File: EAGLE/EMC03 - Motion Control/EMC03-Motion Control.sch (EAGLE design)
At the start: 62 parts, among them J1 HR911105A, J2 SWD, J3 UART0, J6 USB-B, Q2 25MHz, U1 LPC1768, U2 USD-SOCKETSMD, U3 CPL-ETH-PHY-LAN8720A, U4 74LVC1G04, U5 TC1015-3.3VCT713, U6 SP3485

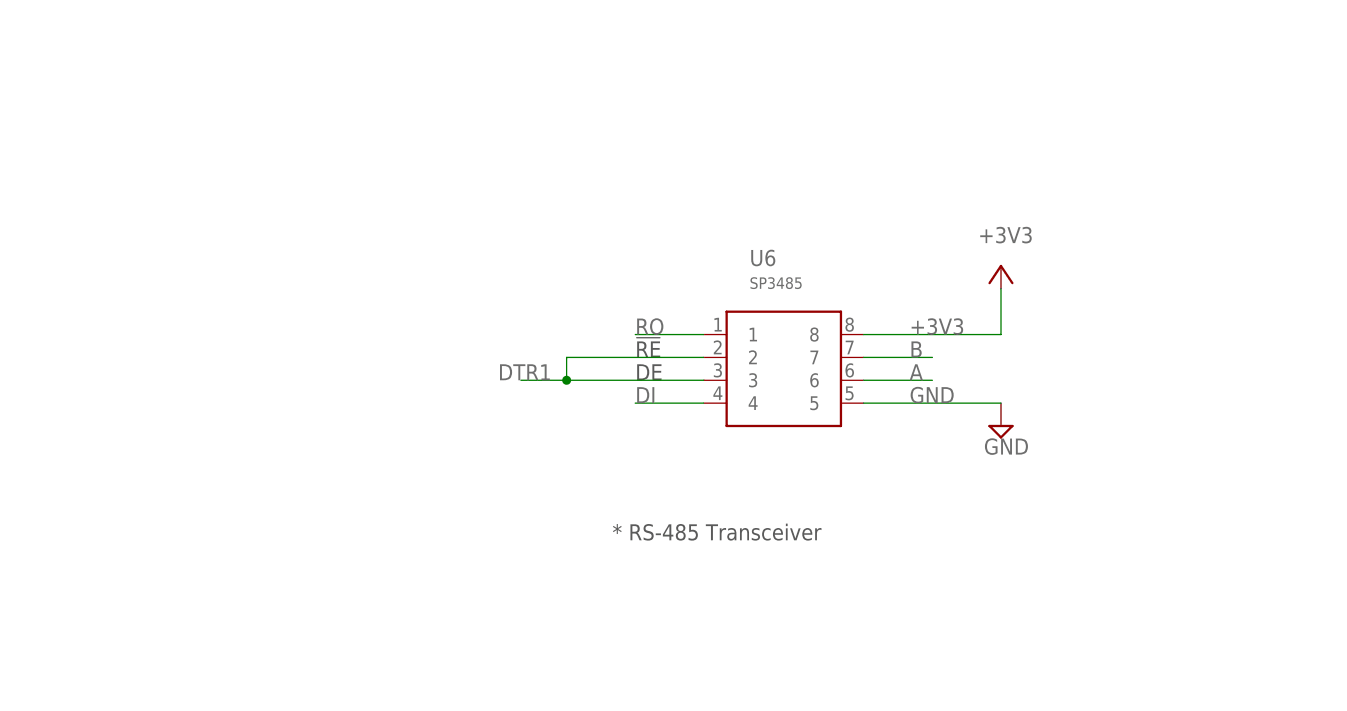
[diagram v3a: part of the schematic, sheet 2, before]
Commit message: Fixed connections for RS-485, added resistors for fail-safe mode and termination. Created RJ-45 device for RS-485 connection. Added LED device and placed on schematic 7 LEDs (4 green, 3 red). Created devices for pushbuttons. Created circuits for DFU and ISP_COM.
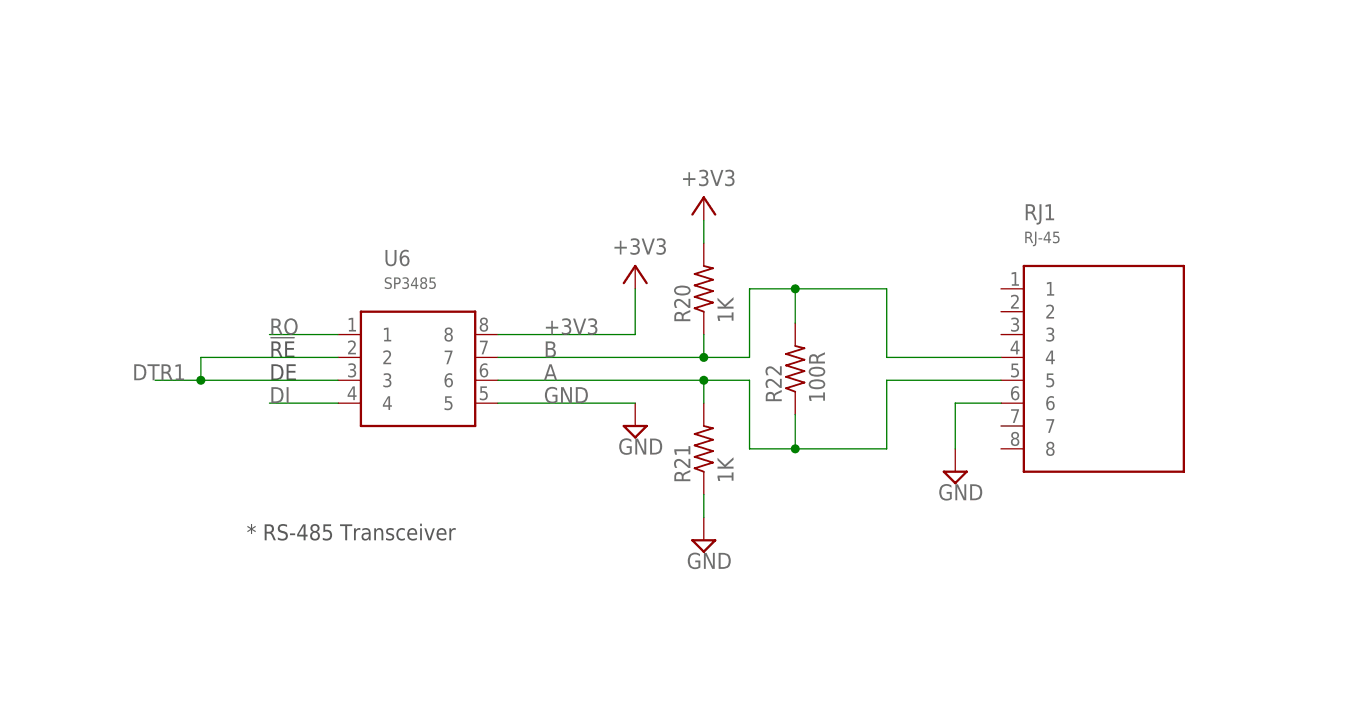
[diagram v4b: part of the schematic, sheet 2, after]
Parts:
- added LED1, LED2, LED3, LED4: GREEN, TinWhiskers:CPL-LED-0603-GREEN
- added LED5, LED6, LED7: RED, TinWhiskers:CPL-LED-0603-RED
- added R20, R21: 1K, TinWhiskers:CPL-RES-0603-1K-0.1W
- added R22: 100R, TinWhiskers:CPL-RES-0603-100-0.1W
- added R23, R24: 10k, TinWhiskers:CPL-RES-0603-10K-0.1W
- added RJ1: RJ-45, TinWhiskers:CPL-CON-MOD-RJ45
- added S2, S3: 147873-2, TinWhiskers:CPL-SW-MOM-0603
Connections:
- new net DFU: R24.1, S3.2, U1.P0-11
- new net ISP_COM: R23.1, S2.2, U1.P0-10
- net +3V3: now also R20.2, R23.2, R24.2
- net A: now also R21.2, R22.1, RJ1.5
- net B: now also R20.1, R22.2, RJ1.4
- net GND: now also R21.1, RJ1.6, S2.1, S3.1
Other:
- moved on the sheet: U6

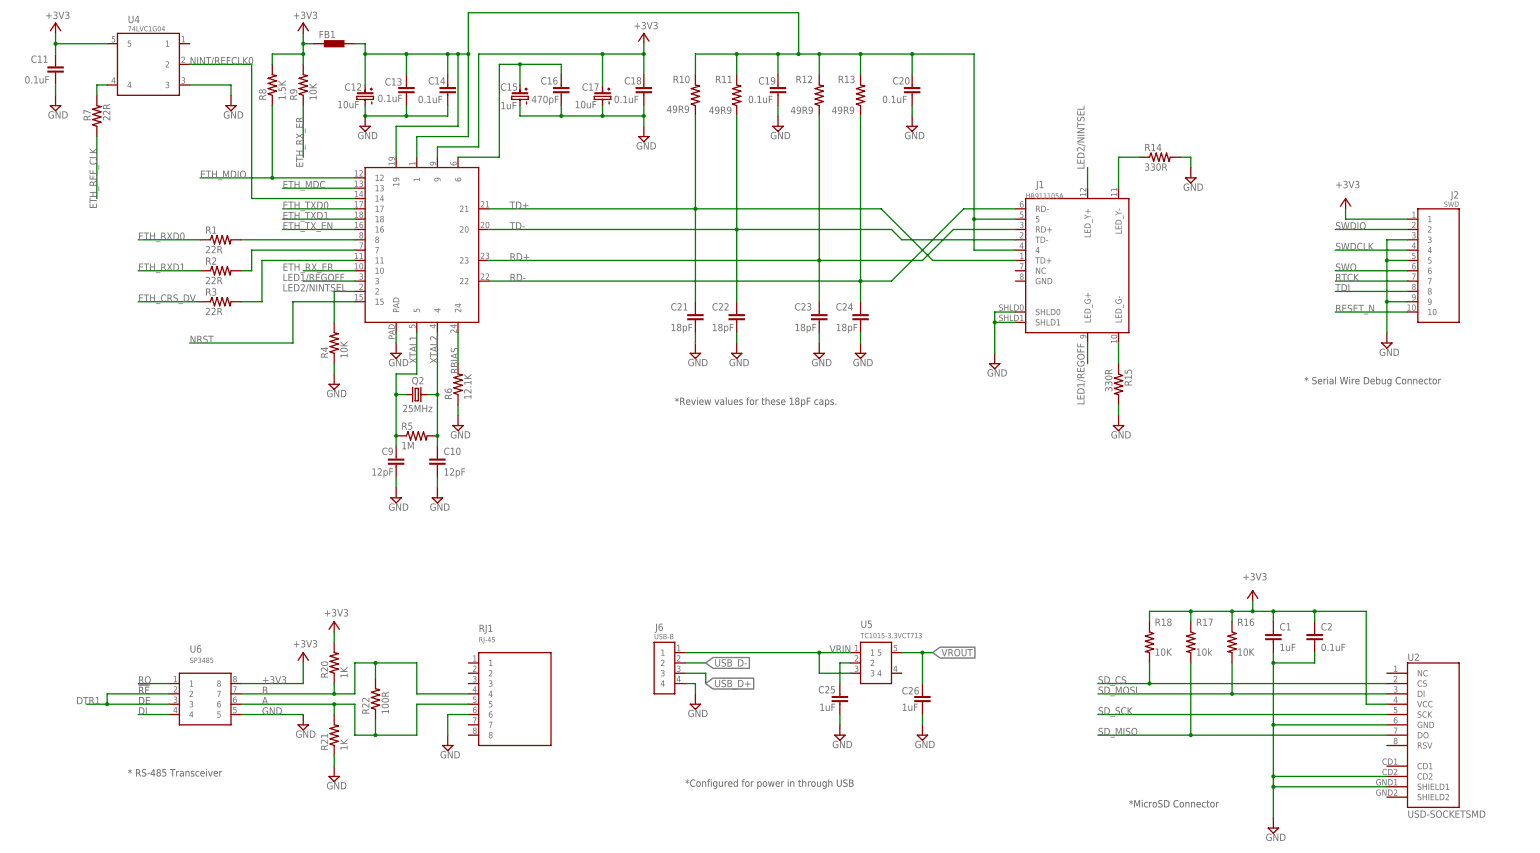
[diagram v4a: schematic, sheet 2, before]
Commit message: Schematic has been updated to assist with sourcing, cleaned up Refdes'.
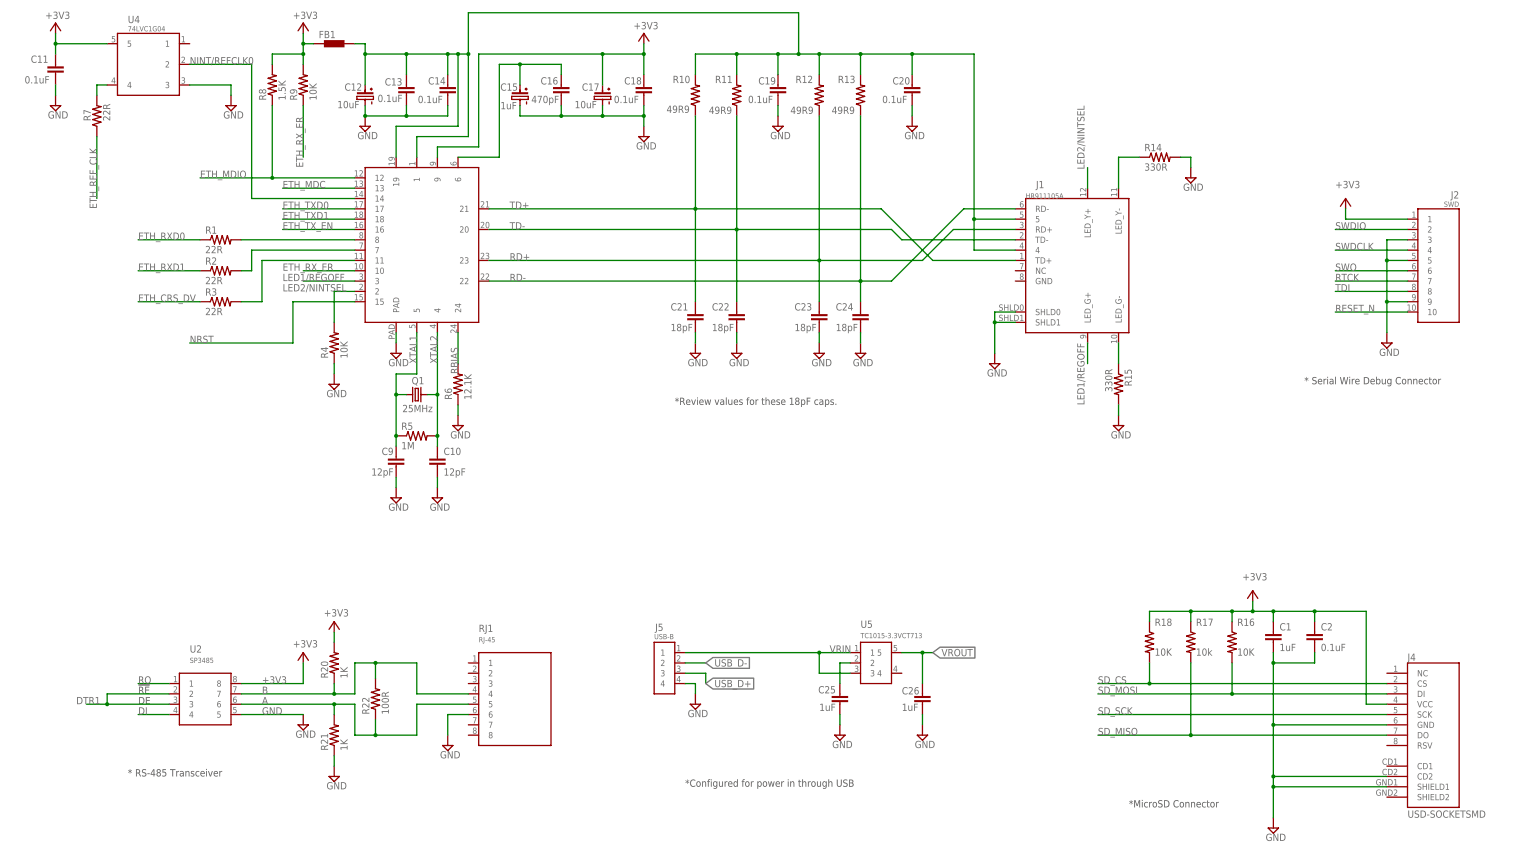
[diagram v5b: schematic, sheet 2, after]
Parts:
- removed U6: SP3485, TinWhiskers:SP3485
- added J4: USD-SOCKETSMD, TinWhiskers:USD-SOCKETSMD
- U2: value USD-SOCKETSMD -> SP3485; device TinWhiskers:USD-SOCKETSMD -> TinWhiskers:SP3485
- renumbered J6 to J5, Q2 to Q1
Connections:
- net +3V3: now also J4.VCC, U2.8; no longer U2.VCC, U6.8
- net A: now also U2.6; no longer U6.6
- net B: now also U2.7; no longer U6.7
- net DI: now also U2.4; no longer U6.4
- net DTR1: now also U2.2, U2.3; no longer U6.2, U6.3
- net GND: now also J4.CD2, J4.GND, J4.SHIELD1, U2.5; no longer U2.CD2, U2.GND, U2.SHIELD1, U6.5
- net RO: now also U2.1; no longer U6.1
- net SD_CS: now also J4.CS; no longer U2.CS
- net SD_MISO: now also J4.DO; no longer U2.DO
- net SD_MOSI: now also J4.DI; no longer U2.DI
- net SD_SCK: now also J4.SCK; no longer U2.SCK
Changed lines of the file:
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@@
 <setting verticaltext="up"/>
 </settings>
-<grid distance="0.1" unitdist="inch" unit="inch" style="lines" multiple="1" display="yes" altdistance="0.025" altunitdist="inch" altunit="inch"/>
+<grid distance="0.1" unitdist="inch" unit="inch" style="lines" multiple="1" display="no" altdistance="0.01" altunitdist="inch" altunit="inch"/>
 <layers>
 <layer number="1" name="Top" color="4" fill="1" visible="no" active="no"/>
@@
 <part name="R3" library="TinWhiskers" deviceset="CPL-RES-0603-22R-0.1W" device="" value="22R"/>
 <part name="SUPPLY3" library="TinWhiskers" deviceset="GND" device=""/>
-<part name="Q2" library="TinWhiskers" deviceset="CPL-OSC-CRY-25MHZ-18PF" device="" value="25MHz"/>
+<part name="Q1" library="TinWhiskers" deviceset="CPL-OSC-CRY-25MHZ-18PF" device="" value="25MHz"/>
 <part name="C9" library="TinWhiskers" deviceset="CPL-CAP-C0G-0603-12PF-50V" device="" value="12pF"/>
 <part name="C10" library="TinWhiskers" deviceset="CPL-CAP-C0G-0603-12PF-50V" device="" value="12pF"/>
@@
 <part name="SUPPLY4" library="TinWhiskers" deviceset="GND" device=""/>
 <part name="SUPPLY5" library="TinWhiskers" deviceset="GND" device=""/>
-<part name="U2" library="TinWhiskers" deviceset="USD-SOCKET" device="SMD"/>
+<part name="J4" library="TinWhiskers" deviceset="USD-SOCKET" device="SMD"/>
 <part name="C1" library="TinWhiskers" deviceset="CPL-CAP-X5R-0603-1UF-50V" device="" value="1uF"/>
 <part name="C2" library="TinWhiskers" deviceset="CPL-CAP-X5R-0603-0.1UF-35V" device="" value="0.1uF"/>
@@
 <part name="+3V4" library="supply1" deviceset="+3V3" device=""/>
 <part name="SUPPLY6" library="TinWhiskers" deviceset="GND" device=""/>
-<part name="J6" library="TinWhiskers" deviceset="CPL-CON-USB-B" device="" value="USB-B"/>
+<part name="J5" library="TinWhiskers" deviceset="CPL-CON-USB-B" device="" value="USB-B"/>
 <part name="U5" library="TinWhiskers" deviceset="CPL-REG-LIN-3.3V-0.1A" device="" value="TC1015-3.3VCT713"/>
 <part name="SUPPLY14" library="TinWhiskers" deviceset="GND" device=""/>
@@
 <part name="+3V5" library="supply1" deviceset="+3V3" device=""/>
 <part name="SUPPLY21" library="TinWhiskers" deviceset="GND" device=""/>
-<part name="U6" library="TinWhiskers" deviceset="SP3485" device=""/>
+<part name="U2" library="TinWhiskers" deviceset="SP3485" device=""/>
 <part name="+3V6" library="supply1" deviceset="+3V3" device=""/>
 <part name="SUPPLY24" library="TinWhiskers" deviceset="GND" device=""/>
@@
 </instance>
 <instance part="SUPPLY3" gate="GND" x="99.06" y="165.1"/>
-<instance part="Q2" gate="G$1" x="104.14" y="154.94" smashed="yes">
+<instance part="Q1" gate="G$1" x="104.14" y="154.94" smashed="yes">
 <attribute name="NAME" x="102.87" y="157.48" size="1.778" layer="95"/>
 <attribute name="VALUE" x="100.584" y="150.622" size="1.778" layer="96"/>
@@
 <instance part="SUPPLY4" gate="GND" x="294.64" y="208.28"/>
 <instance part="SUPPLY5" gate="GND" x="276.86" y="147.32"/>
-<instance part="U2" gate="G$1" x="350.52" y="73.66"/>
+<instance part="J4" gate="G$1" x="350.52" y="73.66"/>
 <instance part="C1" gate="G$1" x="314.96" y="96.52" smashed="yes" rot="R90">
 <attribute name="NAME" x="316.484" y="96.901" size="1.778" layer="95"/>
@@
 </instance>
 <instance part="SUPPLY6" gate="GND" x="314.96" y="48.26"/>
-<instance part="J6" gate="G$1" x="167.64" y="88.9" smashed="yes">
+<instance part="J5" gate="G$1" x="167.64" y="88.9" smashed="yes">
 <attribute name="NAME" x="162.814" y="96.774" size="1.778" layer="95" font="vector" ratio="12"/>
 <attribute name="VALUE" x="162.56" y="94.742" size="1.27" layer="95" font="vector" ratio="10"/>
@@
 </instance>
 <instance part="SUPPLY21" gate="GND" x="342.9" y="167.64"/>
-<instance part="U6" gate="G$1" x="48.26" y="78.74"/>
+<instance part="U2" gate="G$1" x="48.26" y="78.74"/>
 <instance part="+3V6" gate="G$1" x="76.2" y="91.44" smashed="yes">
 <attribute name="VALUE" x="73.66" y="92.71" size="1.778" layer="96"/>
@@
 <junction x="314.96" y="88.9"/>
 <pinref part="SUPPLY6" gate="GND" pin="GND"/>
-<pinref part="U2" gate="G$1" pin="GND"/>
+<pinref part="J4" gate="G$1" pin="GND"/>
 <wire x1="314.96" y1="73.66" x2="314.96" y2="60.96" width="0.1524" layer="91"/>
 <wire x1="314.96" y1="60.96" x2="314.96" y2="58.42" width="0.1524" layer="91"/>
@@
 <wire x1="342.9" y1="73.66" x2="314.96" y2="73.66" width="0.1524" layer="91"/>
 <junction x="314.96" y="73.66"/>
-<pinref part="U2" gate="G$1" pin="CD2"/>
+<pinref part="J4" gate="G$1" pin="CD2"/>
 <wire x1="342.9" y1="60.96" x2="314.96" y2="60.96" width="0.1524" layer="91"/>
 <junction x="314.96" y="60.96"/>
-<pinref part="U2" gate="G$1" pin="SHIELD1"/>
+<pinref part="J4" gate="G$1" pin="SHIELD1"/>
 <wire x1="342.9" y1="58.42" x2="314.96" y2="58.42" width="0.1524" layer="91"/>
 <junction x="314.96" y="58.42"/>
 </segment>
 <segment>
-<pinref part="J6" gate="G$1" pin="4"/>
+<pinref part="J5" gate="G$1" pin="4"/>
 <wire x1="170.18" y1="83.82" x2="172.72" y2="83.82" width="0.1524" layer="91"/>
 <wire x1="172.72" y1="83.82" x2="172.72" y2="81.28" width="0.1524" layer="91"/>
@@
 </segment>
 <segment>
-<pinref part="U6" gate="G$1" pin="5"/>
+<pinref part="U2" gate="G$1" pin="5"/>
 <label x="66.04" y="76.2" size="1.778" layer="95"/>
 <pinref part="SUPPLY24" gate="GND" pin="GND"/>
@@
 <wire x1="104.14" y1="160.02" x2="99.06" y2="160.02" width="0.1524" layer="91"/>
 <wire x1="99.06" y1="160.02" x2="99.06" y2="154.94" width="0.1524" layer="91"/>
-<pinref part="Q2" gate="G$1" pin="1"/>
+<pinref part="Q1" gate="G$1" pin="1"/>
 <wire x1="99.06" y1="154.94" x2="101.6" y2="154.94" width="0.1524" layer="91"/>
 <wire x1="99.06" y1="154.94" x2="99.06" y2="144.78" width="0.1524" layer="91"/>
@@
 <pinref part="U3" gate="G$1" pin="4"/>
 <wire x1="109.22" y1="170.18" x2="109.22" y2="154.94" width="0.1524" layer="91"/>
-<pinref part="Q2" gate="G$1" pin="2"/>
+<pinref part="Q1" gate="G$1" pin="2"/>
 <wire x1="109.22" y1="154.94" x2="106.68" y2="154.94" width="0.1524" layer="91"/>
 <wire x1="109.22" y1="154.94" x2="109.22" y2="144.78" width="0.1524" layer="91"/>
@@
 </segment>
 <segment>
-<pinref part="U2" gate="G$1" pin="VCC"/>
+<pinref part="J4" gate="G$1" pin="VCC"/>
 <wire x1="342.9" y1="78.74" x2="337.82" y2="78.74" width="0.1524" layer="91"/>
 <wire x1="337.82" y1="78.74" x2="337.82" y2="101.6" width="0.1524" layer="91"/>
@@
 <pinref part="+3V6" gate="G$1" pin="+3V3"/>
 <wire x1="76.2" y1="88.9" x2="76.2" y2="83.82" width="0.1524" layer="91"/>
-<pinref part="U6" gate="G$1" pin="8"/>
+<pinref part="U2" gate="G$1" pin="8"/>
 <label x="66.04" y="83.82" size="1.778" layer="95"/>
 <wire x1="76.2" y1="83.82" x2="60.96" y2="83.82" width="0.1524" layer="91"/>
@@
 <net name="SD_CS" class="0">
 <segment>
-<pinref part="U2" gate="G$1" pin="CS"/>
+<pinref part="J4" gate="G$1" pin="CS"/>
 <wire x1="342.9" y1="83.82" x2="284.48" y2="83.82" width="0.1524" layer="91"/>
 <pinref part="R18" gate="G$1" pin="2"/>
@@
 <net name="SD_MOSI" class="0">
 <segment>
-<pinref part="U2" gate="G$1" pin="DI"/>
+<pinref part="J4" gate="G$1" pin="DI"/>
 <wire x1="342.9" y1="81.28" x2="304.8" y2="81.28" width="0.1524" layer="91"/>
 <pinref part="R16" gate="G$1" pin="2"/>
@@
 <net name="SD_SCK" class="0">
 <segment>
-<pinref part="U2" gate="G$1" pin="SCK"/>
+<pinref part="J4" gate="G$1" pin="SCK"/>
 <wire x1="342.9" y1="76.2" x2="271.78" y2="76.2" width="0.1524" layer="91"/>
 <label x="271.78" y="76.2" size="1.778" layer="95"/>
@@
 <net name="SD_MISO" class="0">
 <segment>
-<pinref part="U2" gate="G$1" pin="DO"/>
+<pinref part="J4" gate="G$1" pin="DO"/>
 <wire x1="342.9" y1="71.12" x2="294.64" y2="71.12" width="0.1524" layer="91"/>
 <pinref part="R17" gate="G$1" pin="2"/>
@@
 <net name="VRIN" class="0">
 <segment>
-<pinref part="J6" gate="G$1" pin="1"/>
+<pinref part="J5" gate="G$1" pin="1"/>
 <pinref part="U5" gate="G$1" pin="1"/>
 <wire x1="170.18" y1="91.44" x2="203.2" y2="91.44" width="0.1524" layer="91"/>
@@
 <net name="USB_D-" class="0">
 <segment>
-<pinref part="J6" gate="G$1" pin="2"/>
+<pinref part="J5" gate="G$1" pin="2"/>
 <wire x1="170.18" y1="88.9" x2="175.26" y2="88.9" width="0.1524" layer="91"/>
 <label x="175.26" y="88.9" size="1.778" layer="95" xref="yes"/>
@@
 <net name="USB_D+" class="0">
 <segment>
-<pinref part="J6" gate="G$1" pin="3"/>
+<pinref part="J5" gate="G$1" pin="3"/>
 <wire x1="170.18" y1="86.36" x2="175.26" y2="86.36" width="0.1524" layer="91"/>
 <wire x1="175.26" y1="86.36" x2="175.26" y2="83.82" width="0.1524" layer="91"/>
@@
 <net name="RO" class="0">
 <segment>
-<pinref part="U6" gate="G$1" pin="1"/>
+<pinref part="U2" gate="G$1" pin="1"/>
 <wire x1="43.18" y1="83.82" x2="35.56" y2="83.82" width="0.1524" layer="91"/>
 <label x="35.56" y="83.82" size="1.778" layer="95"/>
@@
 <net name="DTR1" class="0">
 <segment>
-<pinref part="U6" gate="G$1" pin="3"/>
-<pinref part="U6" gate="G$1" pin="2"/>
+<pinref part="U2" gate="G$1" pin="3"/>
+<pinref part="U2" gate="G$1" pin="2"/>
 <wire x1="43.18" y1="81.28" x2="27.94" y2="81.28" width="0.1524" layer="91"/>
 <wire x1="27.94" y1="81.28" x2="27.94" y2="78.74" width="0.1524" layer="91"/>
@@
 <net name="DI" class="0">
 <segment>
-<pinref part="U6" gate="G$1" pin="4"/>
+<pinref part="U2" gate="G$1" pin="4"/>
 <wire x1="43.18" y1="76.2" x2="35.56" y2="76.2" width="0.1524" layer="91"/>
 <label x="35.56" y="76.2" size="1.778" layer="95"/>
@@
 <net name="B" class="0">
 <segment>
-<pinref part="U6" gate="G$1" pin="7"/>
+<pinref part="U2" gate="G$1" pin="7"/>
 <label x="66.04" y="81.28" size="1.778" layer="95"/>
 <wire x1="60.96" y1="81.28" x2="83.82" y2="81.28" width="0.1524" layer="91"/>
@@
 <net name="A" class="0">
 <segment>
-<pinref part="U6" gate="G$1" pin="6"/>
+<pinref part="U2" gate="G$1" pin="6"/>
 <label x="66.04" y="78.74" size="1.778" layer="95"/>
 <wire x1="60.96" y1="78.74" x2="83.82" y2="78.74" width="0.1524" layer="91"/>
